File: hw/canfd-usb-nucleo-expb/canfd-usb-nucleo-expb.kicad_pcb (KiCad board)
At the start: 2 copper layers, 70 x 59 mm, 58 parts, among them CN1 Conn_02x19_Odd_Even, CN2 CONN, J1 USB_C_Receptacle_USB2.0, J2 Conn_01x10, J3 Conn_01x10, J4 Conn_01x10, SW1 SW_Push_Dual_x2, SW2 SW_Push_Dual_x2, SW3 SW_Push_Dual_x2, U1 USBLC6-2SC6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

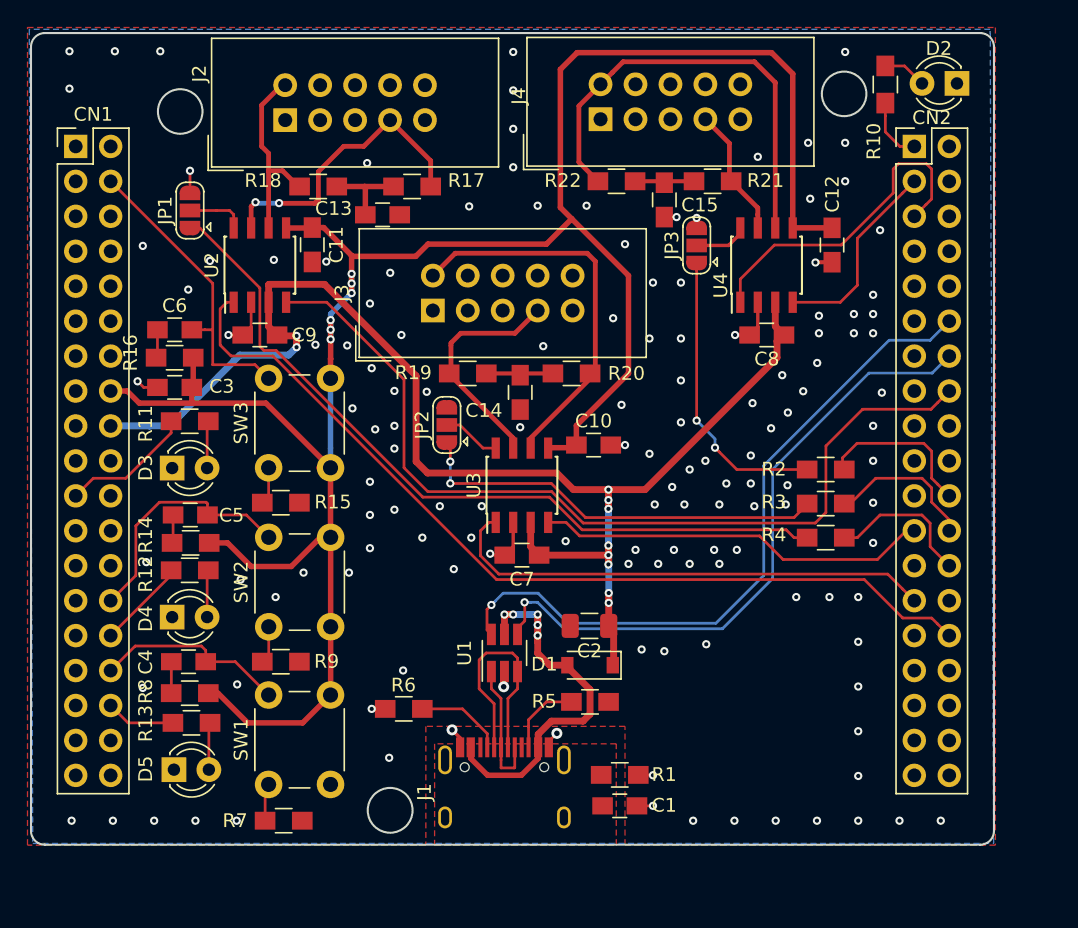
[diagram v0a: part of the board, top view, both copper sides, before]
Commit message: HW: PCB small-fix
Added thermal reliefs to Solder-Jumpers
Slightly moved J2 and J4 to make clearence for mounting holes
Moved R10 for the same reason

Signed-off-by: AlexeyZ <silkt207@gmail.com>
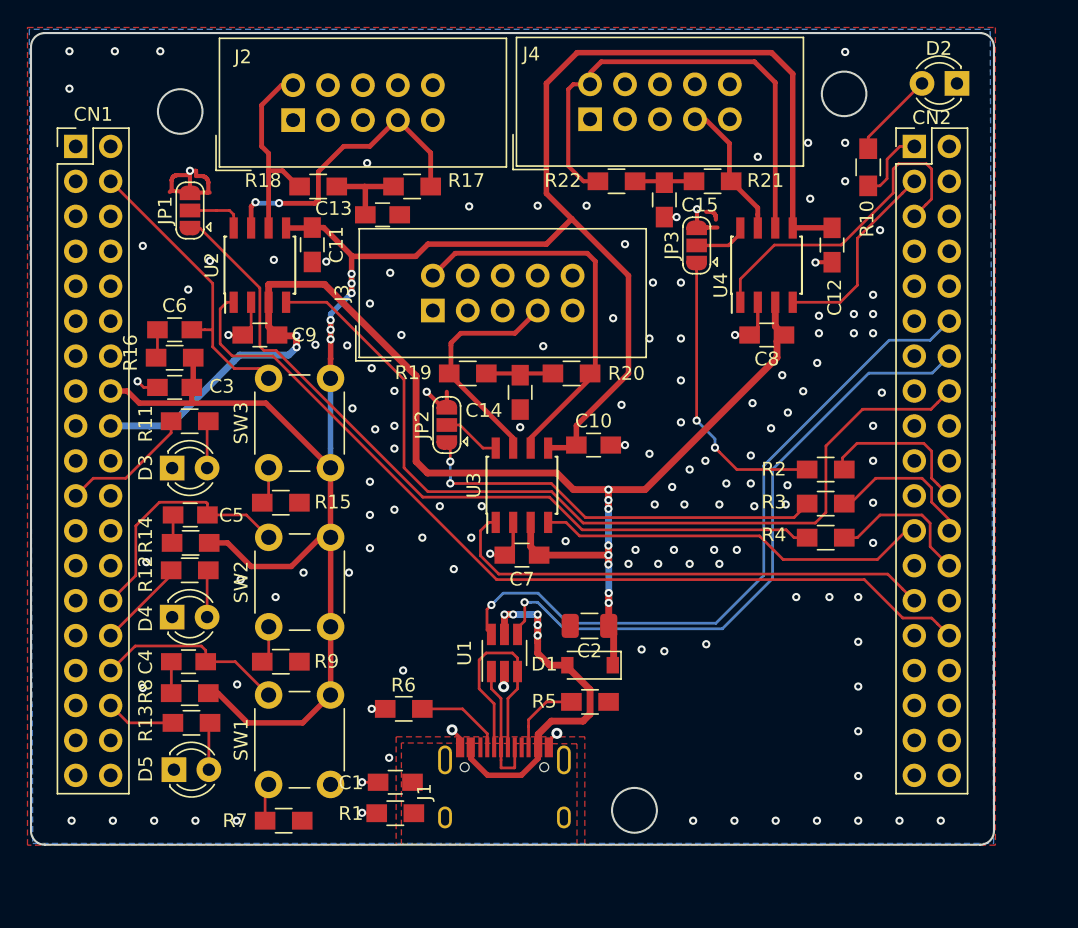
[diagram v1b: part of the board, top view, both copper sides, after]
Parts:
- moved R1 16.6 mm to (128.7, 126.6), turned to 0 degrees
- moved C1 16.4 mm to (128.7, 124.3), turned to 180 degrees
- moved R10 6.14 mm to (163.1, 79.6)
- moved J4 0.76 mm to (142.9, 76.1)
- moved J2 0.57 mm to (121.3, 76.2)
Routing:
- net GND: track 25.5 -> 40.6 mm, vias 136 -> 137
- net Net-(D2-Pad2): track 3.19 -> 6.37 mm
- net CAN3_N: track 32.9 -> 35.8 mm
- net +3V3: track 166.8 -> 167.6 mm
- net SW3: track 25.1 -> 24.4 mm
- net LED1: track 4.64 -> 5.37 mm
- net (no net): vias 6 -> 1
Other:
- outline, holes or cut-outs redrawn
